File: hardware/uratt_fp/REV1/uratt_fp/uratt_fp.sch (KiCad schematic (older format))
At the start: 27 parts, among them J1 Conn_01x10, Q1 DMP31D0U, Q2 2N7002, SW1 SW_Push

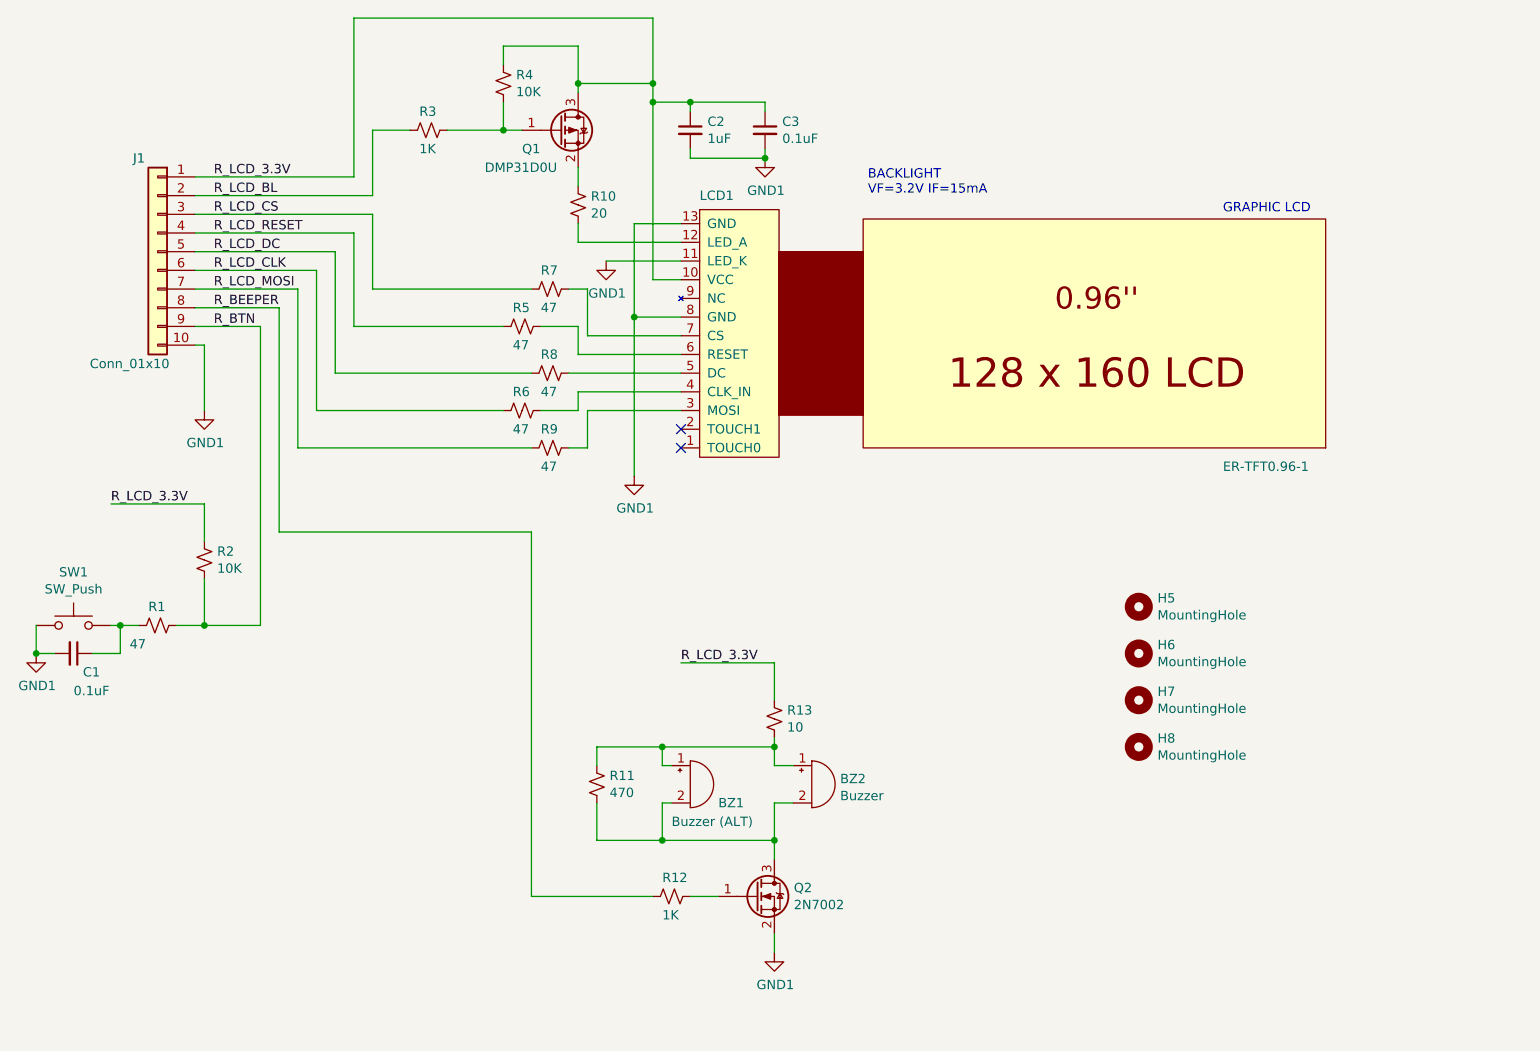
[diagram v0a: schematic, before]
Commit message: separate front panel board layout
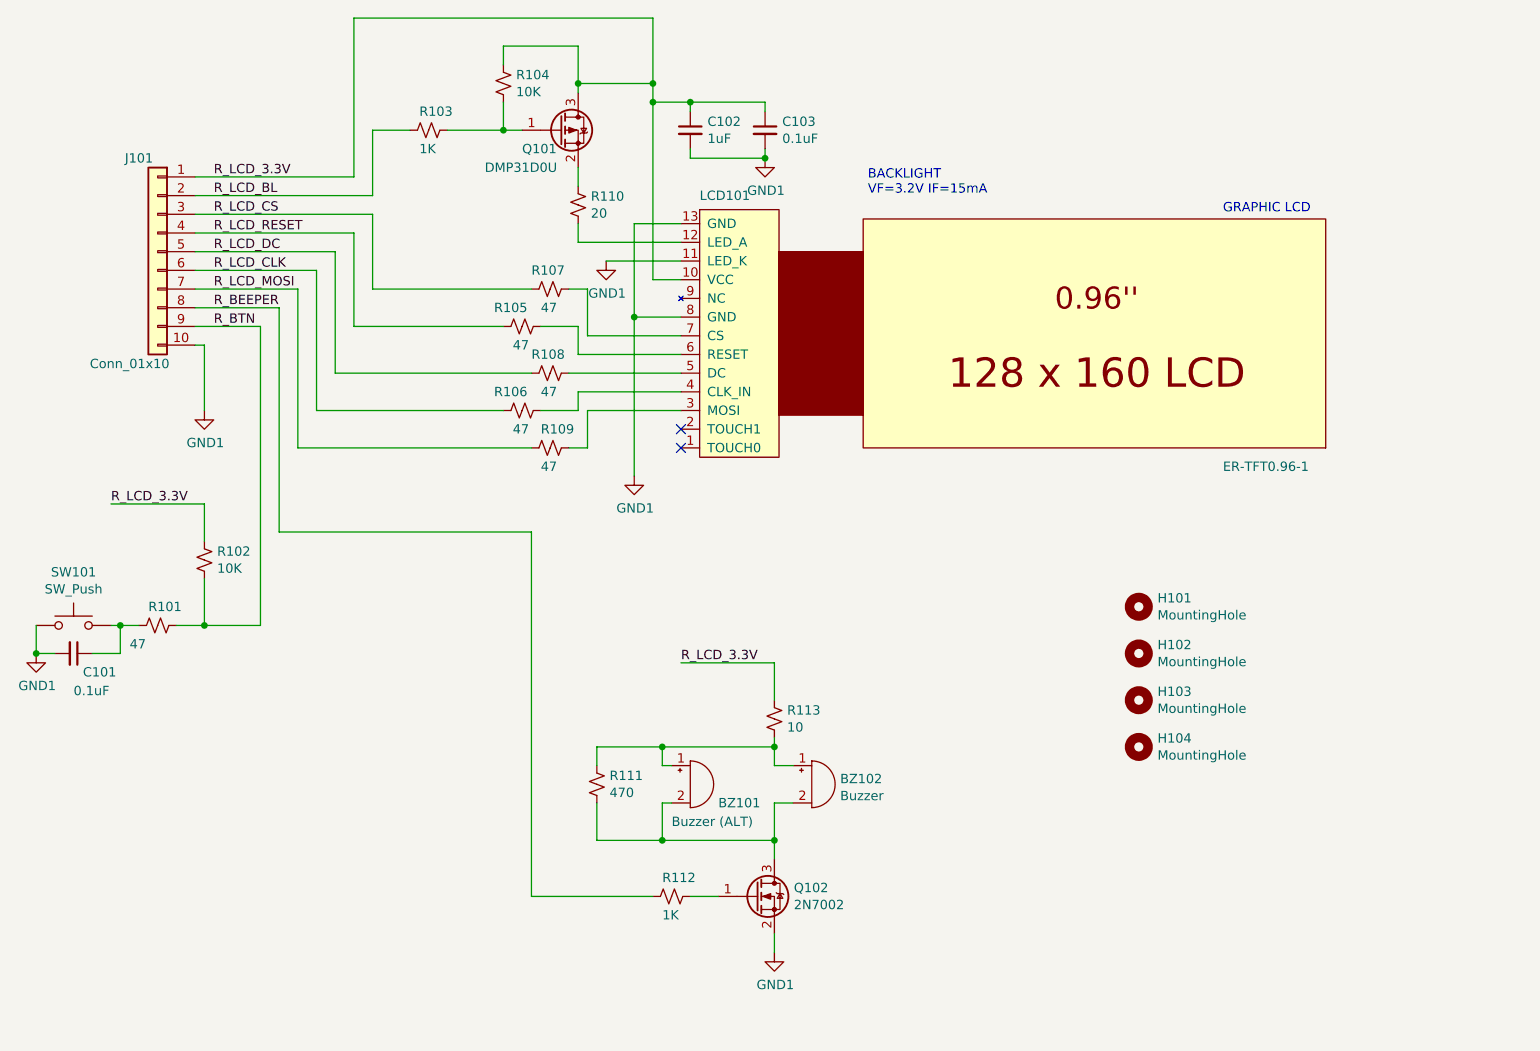
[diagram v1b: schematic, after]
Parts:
- renumbered BZ1 to BZ101, BZ2 to BZ102, C1 to C101, C2 to C102, C3 to C103, H5 to H101, H6 to H102, H7 to H103, H8 to H104, J1 to J101, LCD1 to LCD101, Q1 to Q101, Q2 to Q102, R1 to R101, R2 to R102, R3 to R103, R4 to R104, R5 to R105, R6 to R106, R7 to R107, R8 to R108, R9 to R109, R10 to R110, R11 to R111, R12 to R112, R13 to R113, SW1 to SW101

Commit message: uratt fp, add rails, fiducials, alt speaker option, cap, nearly ready for fab
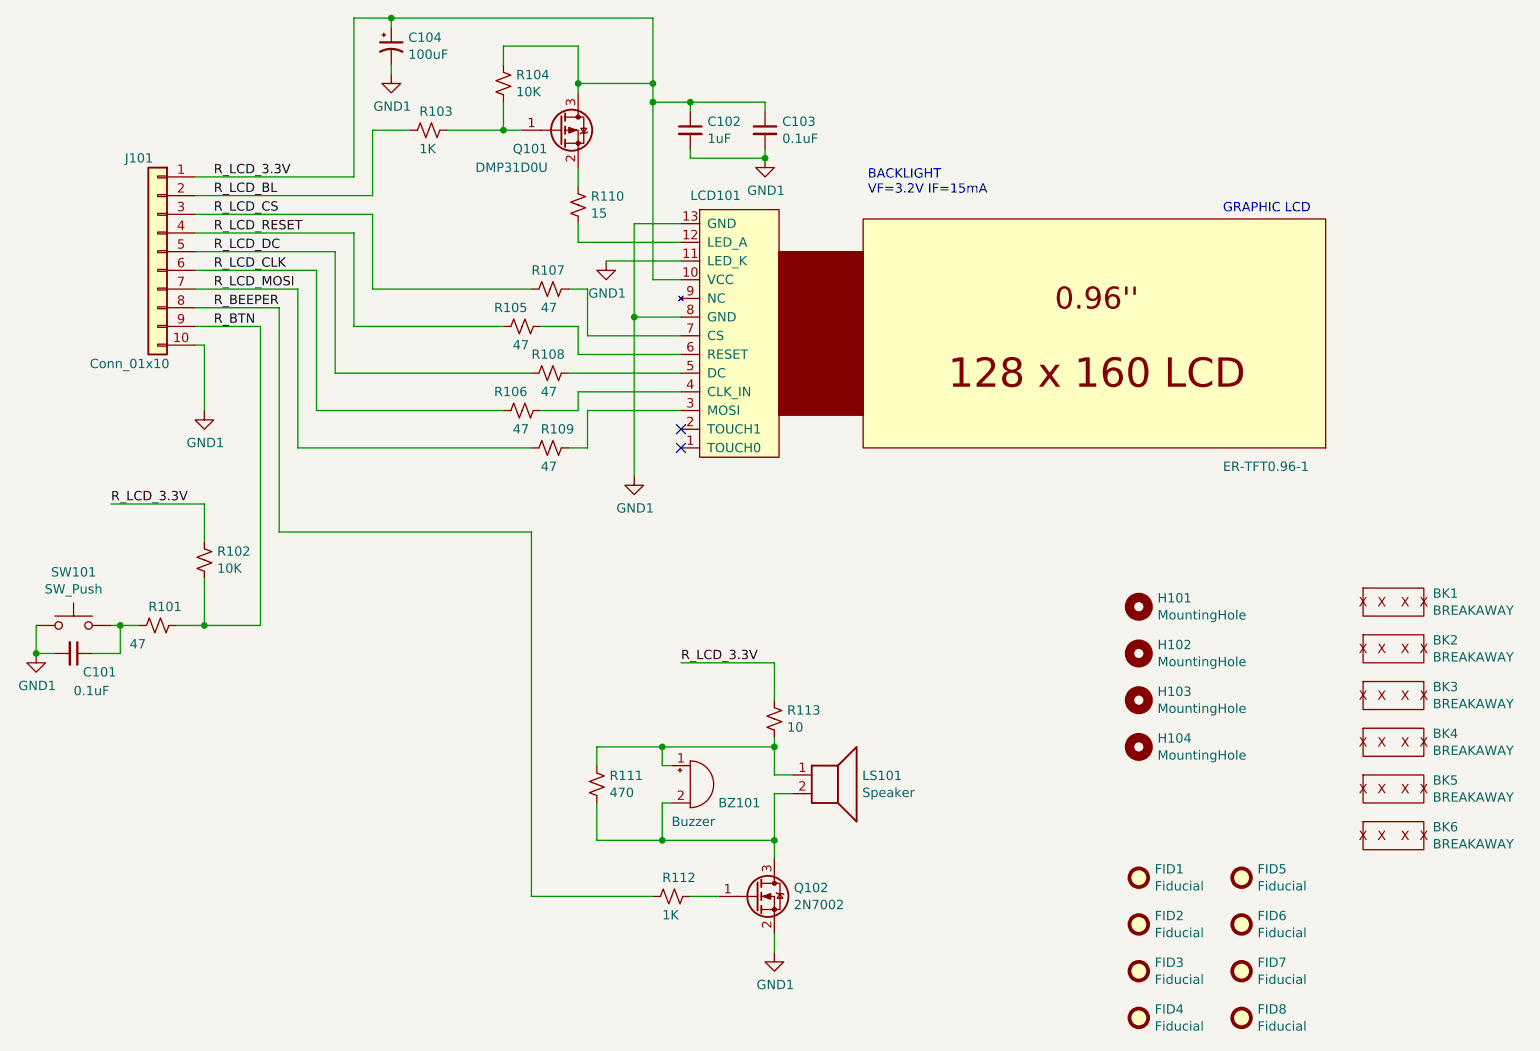
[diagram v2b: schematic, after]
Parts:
- removed BZ102: Buzzer, Buzzer_Beeper:Buzzer_CUI_CPT-9019S-SMT, symbol Device:Buzzer
- added BK1, BK2, BK3, BK4, BK5, BK6: BREAKAWAY, uratt_fp:RATT_BITE, symbol uratt:BREAKAWAY
- added C104: 100uF, Capacitor_SMD:CP_Elec_5x3, symbol Device:CP1_Small
- added FID1, FID2, FID3, FID4, FID5, FID6, FID7, FID8: Fiducial, Fiducial:Fiducial_1.5mm_Mask3mm, symbol Mechanical:Fiducial
- added LS101: Speaker, uratt_fp:SPKR_CVS-1508, symbol Device:Speaker
- BZ101: value Buzzer (ALT) -> Buzzer
- R110: value 20 -> 15
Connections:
- net GND1: now also C104.2
- net R_LCD_3.3V: now also C104.1
- net at BZ101.1 (-), R111.1, R113.2: now also LS101.1
- net at BZ101.2 (+), Q102.3 (D), R111.2: now also LS101.2
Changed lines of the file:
@@
 AR Path="/62F12C4B" Ref="LCD101"  Part="1"
 AR Path="/62EF036B/62F12C4B" Ref="LCD?"  Part="1"
-F 0 "LCD101" H 5800 1700 50  0000 L CNN
+F 0 "LCD101" H 5750 1700 50  0000 L CNN
 F 1 "ER-TFT0.96-1" H 8600 250 50  0000 L CNN
 F 2 "uratt_fp:ER-TFT0.96-1" H 5750 1825 50  0001 C CNN
@@
 AR Path="/62F12C68" Ref="Q101"  Part="1"
 AR Path="/62EF036B/62F12C68" Ref="Q?"  Part="1"
-F 0 "Q101" H 4850 1350 50  0000 L CNN
-F 1 "DMP31D0U" H 4650 1250 50  0000 L CNN
+F 0 "Q101" H 4800 1350 50  0000 L CNN
+F 1 "DMP31D0U" H 4600 1250 50  0000 L CNN
 F 2 "Package_TO_SOT_SMD:SOT-23" H 5250 1375 50  0001 L CIN
 F 3 "https://www.diodes.com/assets/Datasheets/DMP31D0U.pdf" H 5050 1450 50  0001 L CNN
@@
 AR Path="/62EF036B/62F12C6E" Ref="R?"  Part="1"
 F 0 "R110" H 5218 1896 50  0000 L CNN
-F 1 "20" H 5218 1805 50  0000 L CNN
+F 1 "15" H 5218 1805 50  0000 L CNN
 F 2 "Resistor_SMD:R_0603_1608Metric" H 5150 1850 50  0001 C CNN
 F 3 "~" H 5150 1850 50  0001 C CNN
@@
 	3950 1700 3950 850
 Wire Wire Line
-	3950 850  5550 850
+	3950 850  4150 850
 Wire Wire Line
 	5550 850  5550 1200
@@
 Text Label 3200 2500 0    50   ~ 0
 R_BTN
-$Comp
-L Device:Buzzer BZ102
-U 1 1 60451D70
-P 6400 4950
-AR Path="/60451D70" Ref="BZ102"  Part="1"
-AR Path="/62EF036B/60451D70" Ref="BZ?"  Part="1"
-F 0 "BZ102" H 6552 4979 50  0000 L CNN
-F 1 "Buzzer" H 6552 4888 50  0000 L CNN
-F 2 "Buzzer_Beeper:Buzzer_CUI_CPT-9019S-SMT" V 6375 5050 50  0001 C CNN
-F 3 "https://www.cuidevices.com/product/resource/cpt-9019s-smt-tr.pdf" V 6375 5050 50  0001 C CNN
-F 4 "" H 6400 4950 50  0001 C CNN "Field4"
-F 5 "102-3761-1-ND" H 6400 4950 50  0001 C CNN "Digikey"
-	1    6400 4950
-	1    0    0    -1
-$EndComp
-Wire Wire Line
-	6300 4850 6200 4850
-Wire Wire Line
-	6200 4850 6200 4750
+Wire Wire Line
+	6300 4900 6200 4900
+Wire Wire Line
+	6200 4900 6200 4750
 Wire Wire Line
 	6200 5350 6200 5250
 Wire Wire Line
-	6200 5050 6300 5050
+	6200 5000 6300 5000
 $Comp
 L Device:R_Small_US R113
@@
 AR Path="/62EF036B/5FF0EFC7" Ref="BZ?"  Part="1"
 F 0 "BZ101" H 5900 4850 50  0000 L CNN
-F 1 "Buzzer (ALT)" H 5650 4750 50  0000 L CNN
+F 1 "Buzzer" H 5650 4750 50  0000 L CNN
 F 2 "Buzzer_Beeper:Buzzer_CUI_CPT-9019S-SMT" V 5725 5050 50  0001 C CNN
 F 3 "https://www.cuidevices.com/product/resource/cpt-9019s-smt-tr.pdf" V 5725 5050 50  0001 C CNN
@@
 Connection ~ 6200 5250
 Wire Wire Line
-	6200 5250 6200 5050
+	6200 5250 6200 5000
 Wire Wire Line
 	5600 4850 5600 4750
@@
 	1    0    0    -1
 $EndComp
+$Comp
+L uratt:BREAKAWAY BK1
+U 1 1 60033CCA
+P 9350 3900
+F 0 "BK1" H 9723 3871 50  0000 L CNN
+F 1 "BREAKAWAY" H 9723 3780 50  0000 L CNN
+F 2 "uratt_fp:RATT_BITE" H 9350 3900 50  0001 C CNN
+F 3 "" H 9350 3900 50  0001 C CNN
+	1    9350 3900
+	1    0    0    -1
+$EndComp
+$Comp
+L uratt:BREAKAWAY BK2
+U 1 1 60035B74
+P 9350 4150
+F 0 "BK2" H 9723 4121 50  0000 L CNN
+F 1 "BREAKAWAY" H 9723 4030 50  0000 L CNN
+F 2 "uratt_fp:RATT_BITE" H 9350 4150 50  0001 C CNN
+F 3 "" H 9350 4150 50  0001 C CNN
+	1    9350 4150
+	1    0    0    -1
+$EndComp
+$Comp
+L uratt:BREAKAWAY BK3
+U 1 1 60038EFF
+P 9350 4400
+F 0 "BK3" H 9723 4371 50  0000 L CNN
+F 1 "BREAKAWAY" H 9723 4280 50  0000 L CNN
+F 2 "uratt_fp:RATT_BITE" H 9350 4400 50  0001 C CNN
+F 3 "" H 9350 4400 50  0001 C CNN
+	1    9350 4400
+	1    0    0    -1
+$EndComp
+$Comp
+L uratt:BREAKAWAY BK4
+U 1 1 6003C281
+P 9350 4650
+F 0 "BK4" H 9723 4621 50  0000 L CNN
+F 1 "BREAKAWAY" H 9723 4530 50  0000 L CNN
+F 2 "uratt_fp:RATT_BITE" H 9350 4650 50  0001 C CNN
+F 3 "" H 9350 4650 50  0001 C CNN
+	1    9350 4650
+	1    0    0    -1
+$EndComp
+$Comp
+L uratt:BREAKAWAY BK5
+U 1 1 600559B8
+P 9350 4900
+F 0 "BK5" H 9723 4871 50  0000 L CNN
+F 1 "BREAKAWAY" H 9723 4780 50  0000 L CNN
+F 2 "uratt_fp:RATT_BITE" H 9350 4900 50  0001 C CNN
+F 3 "" H 9350 4900 50  0001 C CNN
+	1    9350 4900
+	1    0    0    -1
+$EndComp
+$Comp
+L uratt:BREAKAWAY BK6
+U 1 1 600559BE
+P 9350 5150
+F 0 "BK6" H 9723 5121 50  0000 L CNN
+F 1 "BREAKAWAY" H 9723 5030 50  0000 L CNN
+F 2 "uratt_fp:RATT_BITE" H 9350 5150 50  0001 C CNN
+F 3 "" H 9350 5150 50  0001 C CNN
+	1    9350 5150
+	1    0    0    -1
+$EndComp
+$Comp
+L Mechanical:Fiducial FID1
+U 1 1 60059976
+P 8150 5450
+F 0 "FID1" H 8235 5496 50  0000 L CNN
+F 1 "Fiducial" H 8235 5405 50  0000 L CNN
+F 2 "Fiducial:Fiducial_1.5mm_Mask3mm" H 8150 5450 50  0001 C CNN
+F 3 "~" H 8150 5450 50  0001 C CNN
+	1    8150 5450
+	1    0    0    -1
+$EndComp
+$Comp
+L Mechanical:Fiducial FID2
+U 1 1 6005B080
+P 8150 5700
+F 0 "FID2" H 8235 5746 50  0000 L CNN
+F 1 "Fiducial" H 8235 5655 50  0000 L CNN
+F 2 "Fiducial:Fiducial_1.5mm_Mask3mm" H 8150 5700 50  0001 C CNN
+F 3 "~" H 8150 5700 50  0001 C CNN
+	1    8150 5700
+	1    0    0    -1
+$EndComp
+$Comp
+L Mechanical:Fiducial FID3
+U 1 1 6005E3BB
+P 8150 5950
+F 0 "FID3" H 8235 5996 50  0000 L CNN
+F 1 "Fiducial" H 8235 5905 50  0000 L CNN
+F 2 "Fiducial:Fiducial_1.5mm_Mask3mm" H 8150 5950 50  0001 C CNN
+F 3 "~" H 8150 5950 50  0001 C CNN
+	1    8150 5950
+	1    0    0    -1
+$EndComp
+$Comp
+L Mechanical:Fiducial FID4
+U 1 1 600616B1
+P 8150 6200
+F 0 "FID4" H 8235 6246 50  0000 L CNN
+F 1 "Fiducial" H 8235 6155 50  0000 L CNN
+F 2 "Fiducial:Fiducial_1.5mm_Mask3mm" H 8150 6200 50  0001 C CNN
+F 3 "~" H 8150 6200 50  0001 C CNN
+	1    8150 6200
+	1    0    0    -1
+$EndComp
+$Comp
+L Mechanical:Fiducial FID5
+U 1 1 60071AAA
+P 8700 5450
+F 0 "FID5" H 8785 5496 50  0000 L CNN
+F 1 "Fiducial" H 8785 5405 50  0000 L CNN
+F 2 "Fiducial:Fiducial_1.5mm_Mask3mm" H 8700 5450 50  0001 C CNN
+F 3 "~" H 8700 5450 50  0001 C CNN
+	1    8700 5450
+	1    0    0    -1
+$EndComp
+$Comp
+L Mechanical:Fiducial FID6
+U 1 1 60071AB0
+P 8700 5700
+F 0 "FID6" H 8785 5746 50  0000 L CNN
+F 1 "Fiducial" H 8785 5655 50  0000 L CNN
+F 2 "Fiducial:Fiducial_1.5mm_Mask3mm" H 8700 5700 50  0001 C CNN
+F 3 "~" H 8700 5700 50  0001 C CNN
+	1    8700 5700
+	1    0    0    -1
+$EndComp
+$Comp
+L Mechanical:Fiducial FID7
+U 1 1 60071AB6
+P 8700 5950
+F 0 "FID7" H 8785 5996 50  0000 L CNN
+F 1 "Fiducial" H 8785 5905 50  0000 L CNN
+F 2 "Fiducial:Fiducial_1.5mm_Mask3mm" H 8700 5950 50  0001 C CNN
+F 3 "~" H 8700 5950 50  0001 C CNN
+	1    8700 5950
+	1    0    0    -1
+$EndComp
+$Comp
+L Mechanical:Fiducial FID8
+U 1 1 60071ABC
+P 8700 6200
+F 0 "FID8" H 8785 6246 50  0000 L CNN
+F 1 "Fiducial" H 8785 6155 50  0000 L CNN
+F 2 "Fiducial:Fiducial_1.5mm_Mask3mm" H 8700 6200 50  0001 C CNN
+F 3 "~" H 8700 6200 50  0001 C CNN
+	1    8700 6200
+	1    0    0    -1
+$EndComp
+$Comp
+L Device:CP1_Small C104
+U 1 1 6008F309
+P 4150 1000
+F 0 "C104" H 4241 1046 50  0000 L CNN
+F 1 "100uF" H 4241 955 50  0000 L CNN
+F 2 "Capacitor_SMD:CP_Elec_5x3" H 4150 1000 50  0001 C CNN
+F 3 "~" H 4150 1000 50  0001 C CNN
+	1    4150 1000
+	1    0    0    -1
+$EndComp
+Wire Wire Line
+	4150 900  4150 850
+Connection ~ 4150 850
+Wire Wire Line
+	4150 850  5550 850
+$Comp
+L power:GND1 #PWR01
+U 1 1 60094159
+P 4150 1150
+AR Path="/60094159" Ref="#PWR01"  Part="1"
+AR Path="/62EF036B/60094159" Ref="#PWR?"  Part="1"
+F 0 "#PWR01" H 4150 900 50  0001 C CNN
+F 1 "GND1" H 4155 977 50  0000 C CNN
+F 2 "" H 4150 1150 50  0001 C CNN
+F 3 "" H 4150 1150 50  0001 C CNN
+	1    4150 1150
+	1    0    0    -1
+$EndComp
+Wire Wire Line
+	4150 1100 4150 1150
+$Comp
+L Device:Speaker LS101
+U 1 1 600E4D66
+P 6500 4900
+F 0 "LS101" H 6670 4896 50  0000 L CNN
+F 1 "Speaker" H 6670 4805 50  0000 L CNN
+F 2 "uratt_fp:SPKR_CVS-1508" H 6500 4700 50  0001 C CNN
+F 3 "~" H 6490 4850 50  0001 C CNN
+F 4 "102-2498-ND" H 6500 4900 50  0001 C CNN "Field4"
+	1    6500 4900
+	1    0    0    -1
+$EndComp

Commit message: change front panel to 12 pin
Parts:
- J101: footprint uratt_fp:TE_1-1734742-0 -> uratt_fp:TE_1-1734742-2; symbol Connector_Generic:Conn_01x10 -> Connector_Generic:Conn_01x12; Alt MFR Part ZF5S-10-01-T-WT-TR -> (none); Digikey A100293CT-ND -> A100233CT-ND
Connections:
- net GND1: now also J101.11 (Pin_11), J101.12 (Pin_12); no longer J101.10 (Pin_10)
- net R_BEEPER: now also J101.9 (Pin_9); no longer J101.8 (Pin_8)
- net R_BTN: now also J101.10 (Pin_10); no longer J101.9 (Pin_9)
- net R_LCD_3.3V: now also J101.2 (Pin_2)
- net R_LCD_BL: now also J101.3 (Pin_3); no longer J101.2 (Pin_2)
- net R_LCD_CLK: now also J101.7 (Pin_7); no longer J101.6 (Pin_6)
- net R_LCD_CS: now also J101.4 (Pin_4); no longer J101.3 (Pin_3)
- net R_LCD_DC: now also J101.6 (Pin_6); no longer J101.5 (Pin_5)
- net R_LCD_MOSI: now also J101.8 (Pin_8); no longer J101.7 (Pin_7)
- net R_LCD_RESET: now also J101.5 (Pin_5); no longer J101.4 (Pin_4)
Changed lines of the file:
@@
 	4250 1450 4050 1450
 $Comp
-L Connector_Generic:Conn_01x10 J101
+L Connector_Generic:Conn_01x12 J101
 U 1 1 62F12CC7
 P 2900 2100
 AR Path="/62F12CC7" Ref="J101"  Part="1"
 AR Path="/62EF036B/62F12CC7" Ref="J?"  Part="1"
-F 0 "J101" H 3000 2600 50  0000 C CNN
-F 1 "Conn_01x10" H 3050 1500 50  0000 C CNN
-F 2 "uratt_fp:TE_1-1734742-0" H 2900 2100 50  0001 C CNN
+F 0 "J101" H 2900 2700 50  0000 C CNN
+F 1 "Conn_01x10" H 3000 1400 50  0000 C CNN
+F 2 "uratt_fp:TE_1-1734742-2" H 2900 2100 50  0001 C CNN
 F 3 "https://www.te.com/commerce/DocumentDelivery/DDEController?Action=srchrtrv&DocNm=1734839&DocType=Customer+Drawing&DocLang=English" H 2900 2100 50  0001 C CNN
 F 4 "" H 2900 2100 50  0001 C CNN "Field4"
-F 5 "ZF5S-10-01-T-WT-TR" H 2900 2100 50  0001 C CNN "Alt MFR Part"
-F 6 "A100293CT-ND" H 2900 2100 50  0001 C CNN "Digikey"
+F 5 "" H 2900 2100 50  0001 C CNN "Alt MFR Part"
+F 6 "A100233CT-ND" H 2900 2100 50  0001 C CNN "Digikey"
 	1    2900 2100
 	-1   0    0    -1
@@
 	3650 2300 3100 2300
 Wire Wire Line
-	3100 1700 3950 1700
+	3100 1700 3150 1700
 Wire Wire Line
 	3950 1700 3950 850
@@
 	3100 2600 3150 2600
 Wire Wire Line
-	3150 2600 3150 2950
+	3150 2600 3150 2700
 $Comp
 L power:GND1 #PWR0105
@@
 	1    0    0    -1
 $EndComp
+Wire Wire Line
+	3100 1600 3150 1600
+Wire Wire Line
+	3150 1600 3150 1700
+Connection ~ 3150 1700
+Wire Wire Line
+	3150 1700 3950 1700
+Wire Wire Line
+	3100 2700 3150 2700
+Connection ~ 3150 2700
+Wire Wire Line
+	3150 2700 3150 2950
 $EndSCHEMATC
